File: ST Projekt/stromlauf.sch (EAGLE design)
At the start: 44 parts, among them IC1 L293E, T1 2N7002BK, T2 2N7002BK, T3 BSS84AKW, T4 BSS84AKW

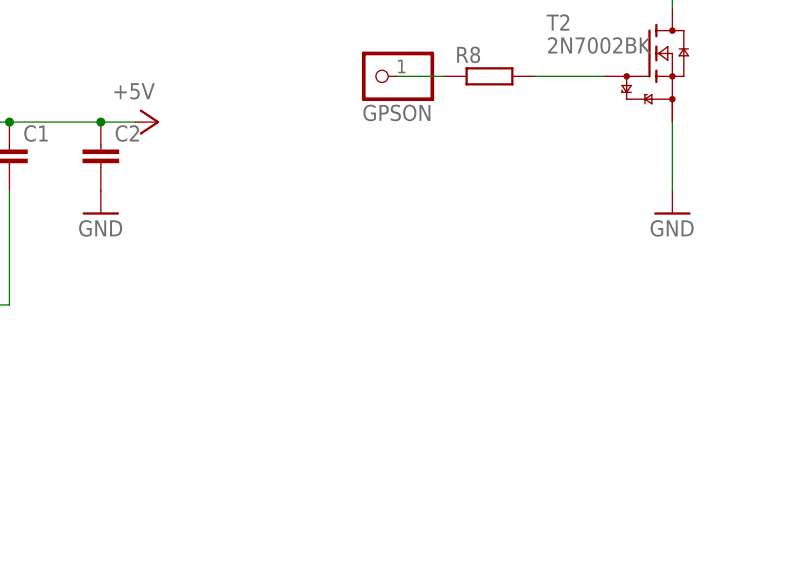
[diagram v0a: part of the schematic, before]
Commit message: Update stromlauf.sch
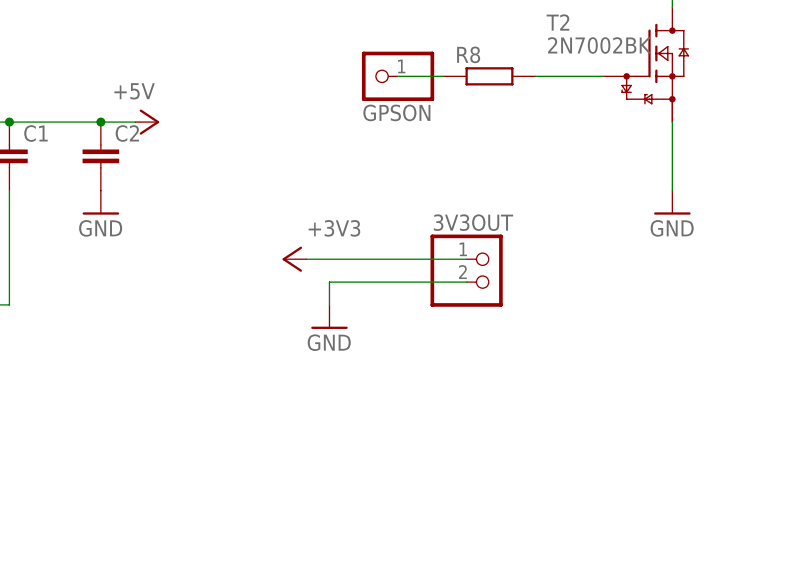
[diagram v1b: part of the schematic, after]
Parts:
- added 3V3OUT: (no value), pinhead:PINHD-1X2
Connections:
- net +3V3: now also 3V3OUT.1
- net GND: now also 3V3OUT.2
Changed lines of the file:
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@@
 <part name="GND19" library="supply1" library_urn="urn:adsk.eagle:library:371" deviceset="GND" device=""/>
 <part name="P+8" library="supply1" library_urn="urn:adsk.eagle:library:371" deviceset="VCC" device=""/>
+<part name="3V3OUT" library="pinhead" library_urn="urn:adsk.eagle:library:325" deviceset="PINHD-1X2" device="" package3d_urn="urn:adsk.eagle:package:22435/2"/>
+<part name="GND20" library="supply1" library_urn="urn:adsk.eagle:library:371" deviceset="GND" device=""/>
+<part name="P+13" library="supply1" library_urn="urn:adsk.eagle:library:371" deviceset="VCC" device=""/>
 </parts>
 <sheets>
@@
 </instance>
 <instance part="P+8" gate="VCC" x="177.8" y="165.1" smashed="yes" rot="R270"/>
+<instance part="3V3OUT" gate="G$1" x="213.36" y="45.72" smashed="yes">
+<attribute name="NAME" x="207.01" y="51.435" size="1.778" layer="95"/>
+<attribute name="VALUE" x="207.01" y="40.64" size="1.778" layer="96"/>
+</instance>
+<instance part="GND20" gate="1" x="195.58" y="40.64" smashed="yes">
+<attribute name="VALUE" x="193.04" y="38.1" size="1.778" layer="96"/>
+</instance>
+<instance part="P+13" gate="VCC" x="190.5" y="48.26" smashed="yes" rot="R90"/>
 </instances>
 <busses>
@@
 <pinref part="GND19" gate="1" pin="GND"/>
 <wire x1="162.56" y1="172.72" x2="172.72" y2="172.72" width="0.1524" layer="91"/>
+</segment>
+<segment>
+<pinref part="3V3OUT" gate="G$1" pin="2"/>
+<wire x1="210.82" y1="45.72" x2="195.58" y2="45.72" width="0.1524" layer="91"/>
+<pinref part="GND20" gate="1" pin="GND"/>
+<wire x1="195.58" y1="45.72" x2="195.58" y2="43.18" width="0.1524" layer="91"/>
 </segment>
 </net>
@@
 <pinref part="L4" gate="G$1" pin="2"/>
 </segment>
+<segment>
+<pinref part="P+13" gate="VCC" pin="VCC"/>
+<pinref part="3V3OUT" gate="G$1" pin="1"/>
+<wire x1="193.04" y1="48.26" x2="210.82" y2="48.26" width="0.1524" layer="91"/>
+<label x="193.04" y="50.8" size="1.778" layer="95"/>
+</segment>
 </net>

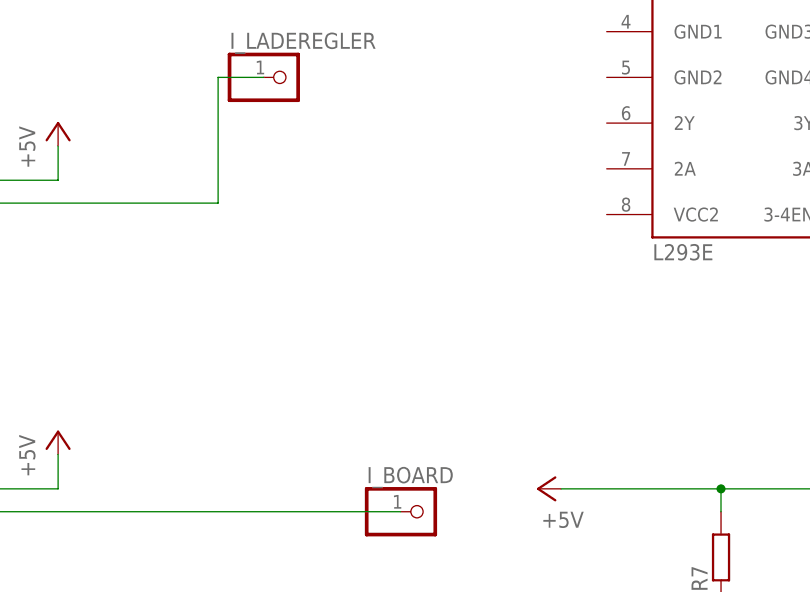
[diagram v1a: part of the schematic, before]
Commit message: Update stromlauf.sch
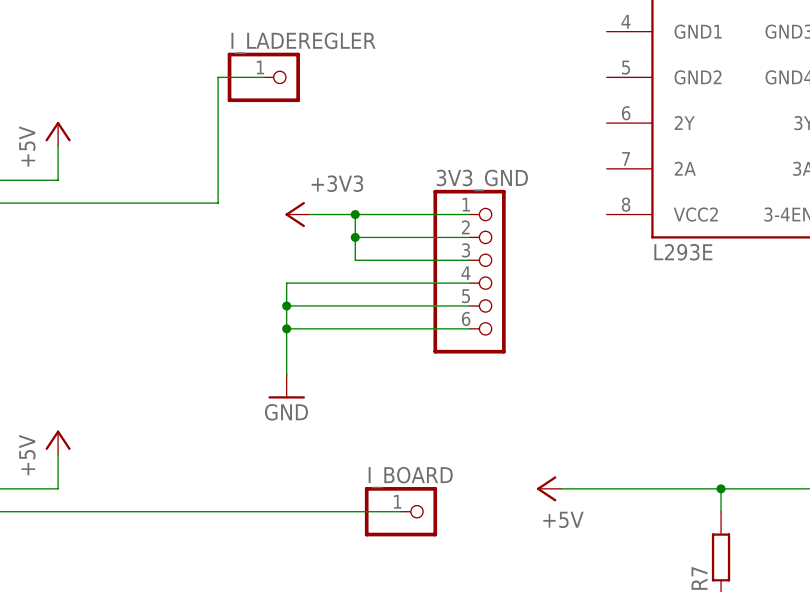
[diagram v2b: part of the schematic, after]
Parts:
- added 3V3_GND: (no value), pinhead:PINHD-1X6
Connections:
- net +3V3: now also 3V3_GND.1, 3V3_GND.2, 3V3_GND.3
- net GND: now also 3V3_GND.4, 3V3_GND.5, 3V3_GND.6
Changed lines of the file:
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@@
 <part name="GND20" library="supply1" library_urn="urn:adsk.eagle:library:371" deviceset="GND" device=""/>
 <part name="P+13" library="supply1" library_urn="urn:adsk.eagle:library:371" deviceset="VCC" device=""/>
+<part name="3V3_GND" library="pinhead" library_urn="urn:adsk.eagle:library:325" deviceset="PINHD-1X6" device="" package3d_urn="urn:adsk.eagle:package:22472/2"/>
+<part name="P+14" library="supply1" library_urn="urn:adsk.eagle:library:371" deviceset="VCC" device=""/>
+<part name="GND21" library="supply1" library_urn="urn:adsk.eagle:library:371" deviceset="GND" device=""/>
 </parts>
 <sheets>
@@
 </instance>
 <instance part="P+13" gate="VCC" x="190.5" y="48.26" smashed="yes" rot="R90"/>
+<instance part="3V3_GND" gate="A" x="187.96" y="124.46" smashed="yes">
+<attribute name="NAME" x="181.61" y="135.255" size="1.778" layer="95"/>
+<attribute name="VALUE" x="181.61" y="114.3" size="1.778" layer="96"/>
+</instance>
+<instance part="P+14" gate="VCC" x="165.1" y="132.08" smashed="yes" rot="R90"/>
+<instance part="GND21" gate="1" x="165.1" y="111.76" smashed="yes">
+<attribute name="VALUE" x="162.56" y="109.22" size="1.778" layer="96"/>
+</instance>
 </instances>
 <busses>
@@
 <pinref part="GND20" gate="1" pin="GND"/>
 <wire x1="195.58" y1="45.72" x2="195.58" y2="43.18" width="0.1524" layer="91"/>
+</segment>
+<segment>
+<pinref part="3V3_GND" gate="A" pin="4"/>
+<pinref part="GND21" gate="1" pin="GND"/>
+<wire x1="185.42" y1="124.46" x2="165.1" y2="124.46" width="0.1524" layer="91"/>
+<wire x1="165.1" y1="124.46" x2="165.1" y2="121.92" width="0.1524" layer="91"/>
+<pinref part="3V3_GND" gate="A" pin="5"/>
+<wire x1="165.1" y1="121.92" x2="165.1" y2="119.38" width="0.1524" layer="91"/>
+<wire x1="165.1" y1="119.38" x2="165.1" y2="114.3" width="0.1524" layer="91"/>
+<wire x1="185.42" y1="121.92" x2="165.1" y2="121.92" width="0.1524" layer="91"/>
+<junction x="165.1" y="121.92"/>
+<pinref part="3V3_GND" gate="A" pin="6"/>
+<wire x1="185.42" y1="119.38" x2="165.1" y2="119.38" width="0.1524" layer="91"/>
+<junction x="165.1" y="119.38"/>
 </segment>
 </net>
@@
 <label x="193.04" y="50.8" size="1.778" layer="95"/>
 </segment>
+<segment>
+<pinref part="3V3_GND" gate="A" pin="1"/>
+<pinref part="P+14" gate="VCC" pin="VCC"/>
+<wire x1="185.42" y1="132.08" x2="172.72" y2="132.08" width="0.1524" layer="91"/>
+<pinref part="3V3_GND" gate="A" pin="2"/>
+<wire x1="172.72" y1="132.08" x2="167.64" y2="132.08" width="0.1524" layer="91"/>
+<wire x1="185.42" y1="129.54" x2="172.72" y2="129.54" width="0.1524" layer="91"/>
+<wire x1="172.72" y1="129.54" x2="172.72" y2="132.08" width="0.1524" layer="91"/>
+<junction x="172.72" y="132.08"/>
+<pinref part="3V3_GND" gate="A" pin="3"/>
+<wire x1="185.42" y1="127" x2="172.72" y2="127" width="0.1524" layer="91"/>
+<wire x1="172.72" y1="127" x2="172.72" y2="129.54" width="0.1524" layer="91"/>
+<junction x="172.72" y="129.54"/>
+<label x="167.64" y="134.62" size="1.778" layer="95"/>
+</segment>
 </net>

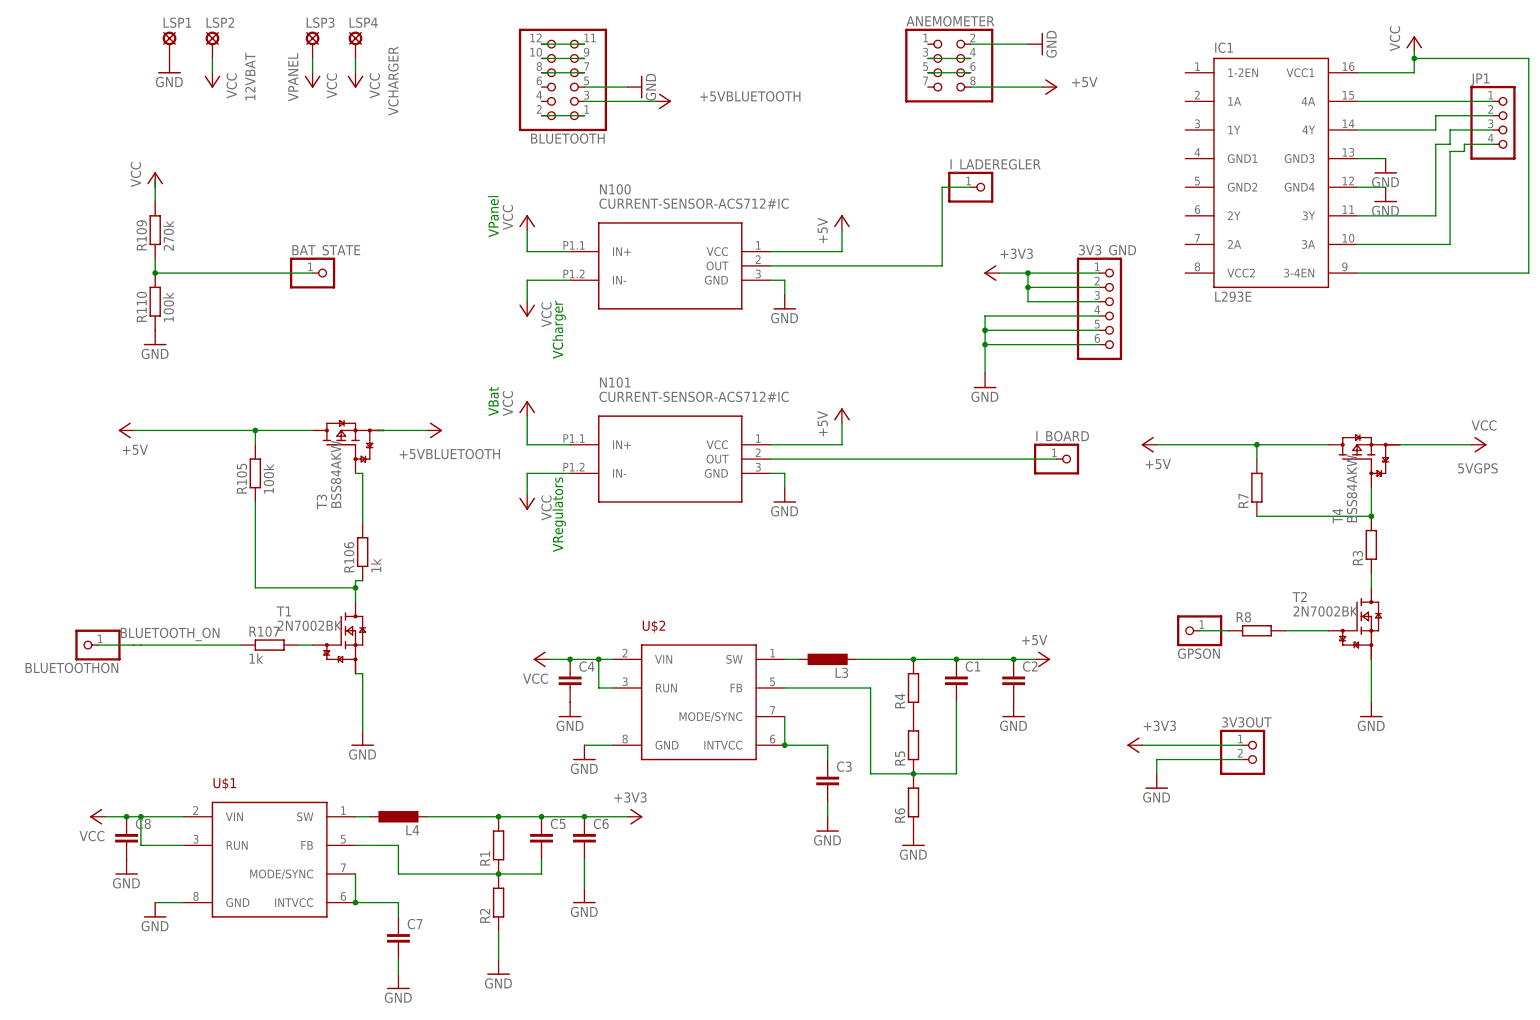
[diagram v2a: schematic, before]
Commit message: Update stromlauf.sch
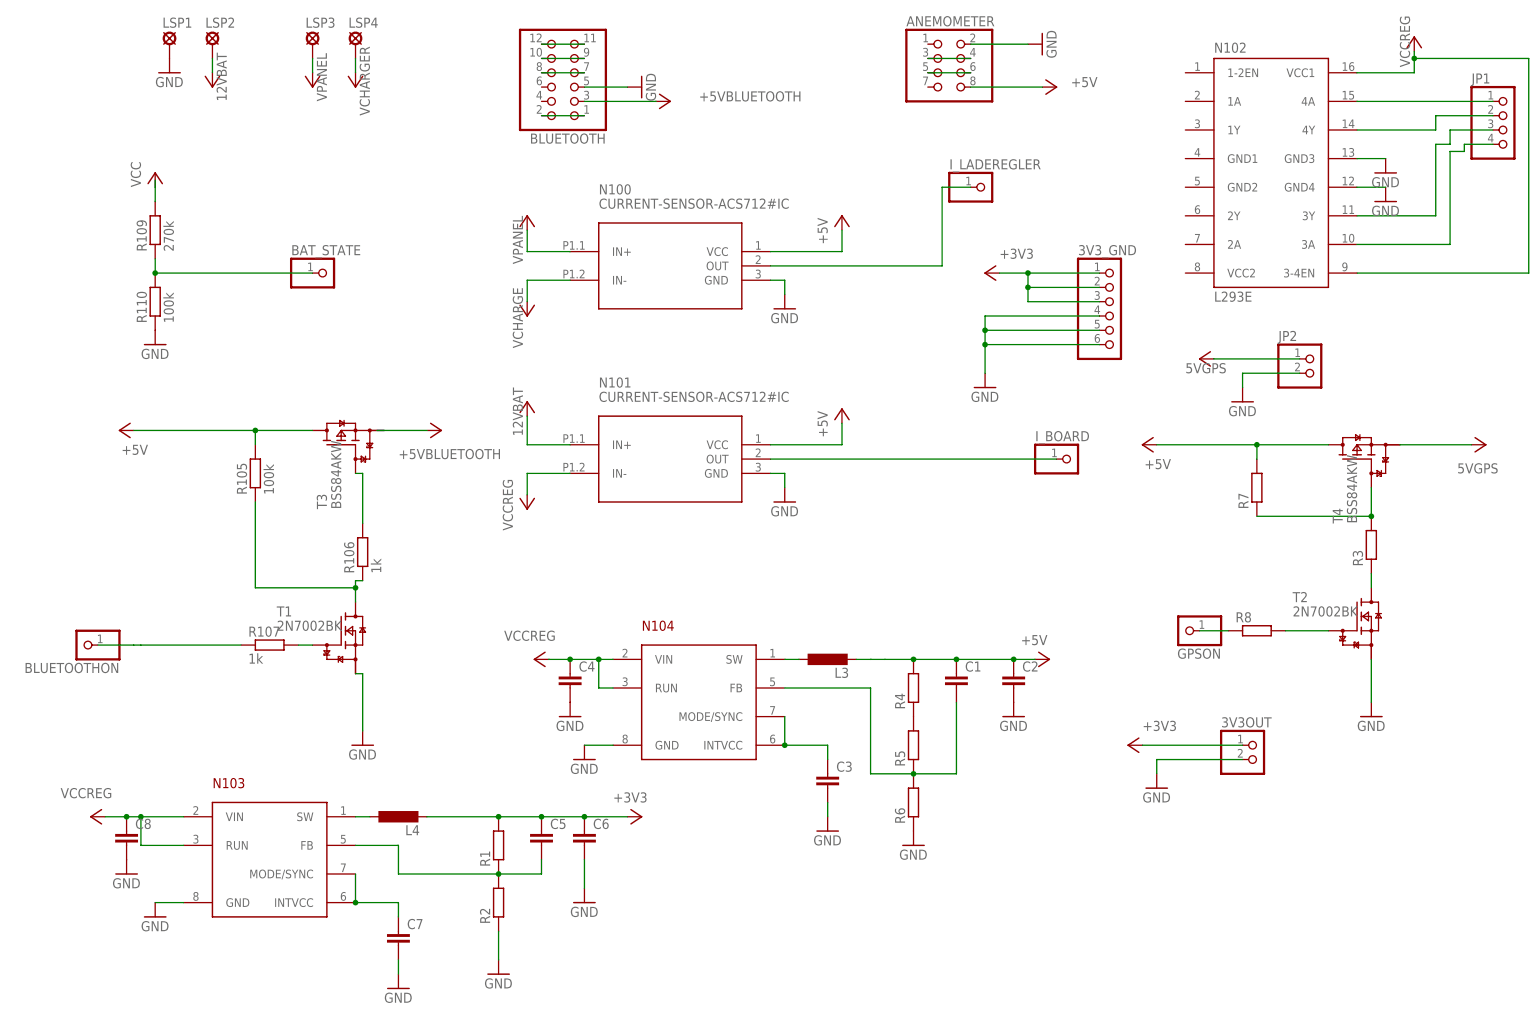
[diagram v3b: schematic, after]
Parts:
- added JP2: (no value), pinhead:PINHD-1X2
- renumbered IC1 to N102, U$1 to N103, U$2 to N104
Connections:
- removed net VCC: C4.1, C8.1, N103.RUN, N103.VIN, N104.RUN, N104.VIN
- net 5VGPS: now also JP2.1
- net GND: now also JP2.2
- net VCCREG: now also C4.1, C8.1, N103.RUN, N103.VIN, N104.RUN, N104.VIN
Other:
- note removed: "VBat"
- note removed: "VCharger"
- note removed: "VPanel"
- note removed: "VRegulators"
